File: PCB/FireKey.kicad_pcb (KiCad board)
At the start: 2 copper layers, 100 x 96.5 mm, 76 parts, among them SW1 SW_MEC_5E, U1 Arduino_Pro_Micro_USB-C

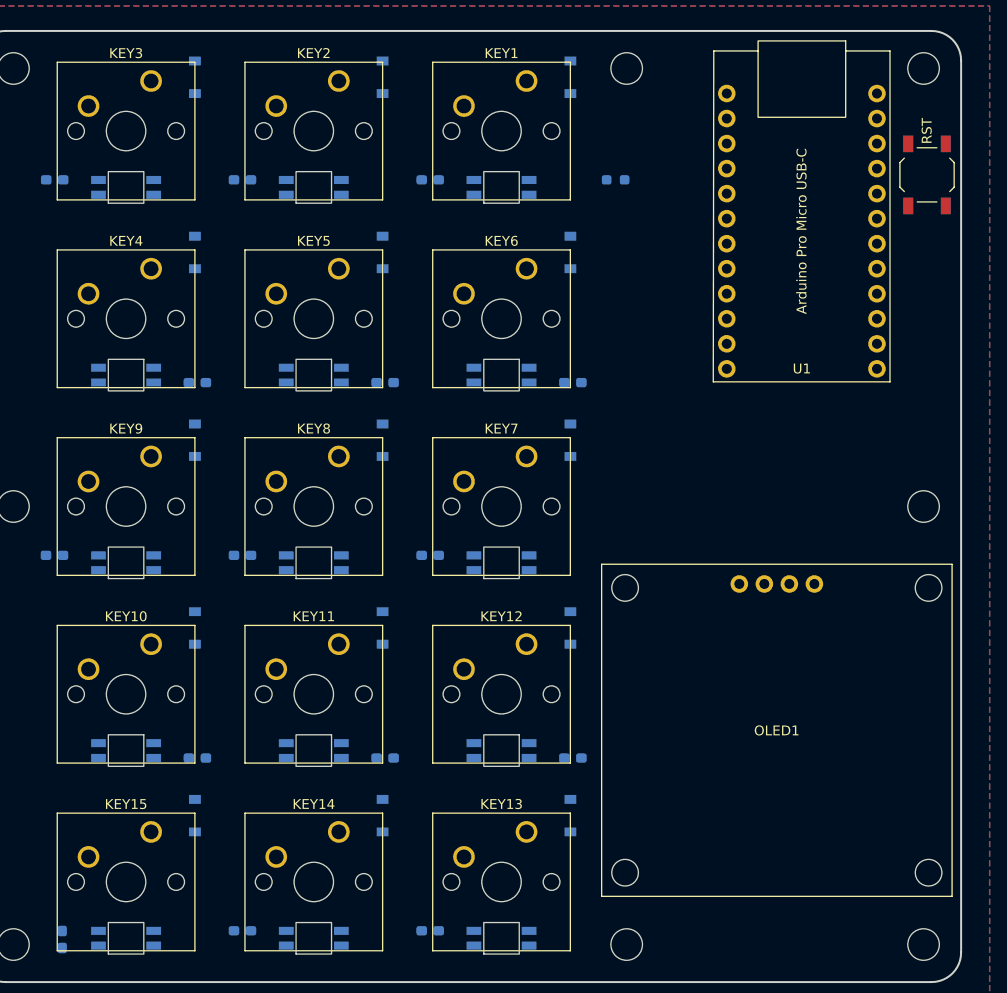
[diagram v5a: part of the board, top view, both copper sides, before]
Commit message: started routing pcb
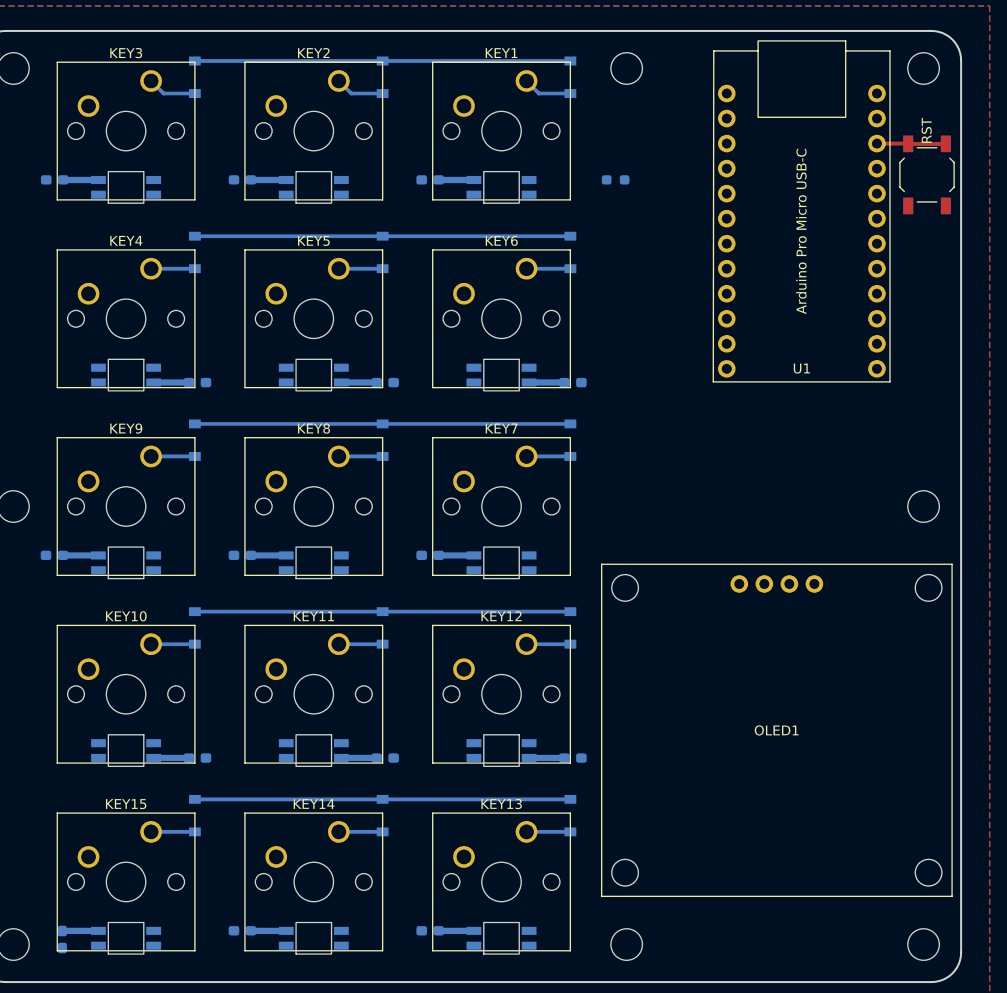
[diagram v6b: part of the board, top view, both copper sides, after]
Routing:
- net VCC: track 0.00 -> 54.2 mm
- net Row4: track 0.00 -> 38.1 mm
- net Row3: track 0.00 -> 38.1 mm
- net Row2: track 0.00 -> 38.1 mm
- net Row1: track 0.00 -> 38.1 mm
- net Row0: track 0.00 -> 38.1 mm
- net RST: track 0.00 -> 6.99 mm
- net Net-(D1-Pad2): track 0.00 -> 4.97 mm
- net Net-(D3-Pad2): track 0.00 -> 4.97 mm
- net Net-(D2-Pad2): track 0.00 -> 4.97 mm
- net Net-(D7-Pad2): track 0.00 -> 4.45 mm
- net Net-(D6-Pad2): track 0.00 -> 4.45 mm
- net Net-(D13-Pad2): track 0.00 -> 4.45 mm
- net Net-(D12-Pad2): track 0.00 -> 4.45 mm
- net Net-(D9-Pad2): track 0.00 -> 4.44 mm
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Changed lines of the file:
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@@
     (effects (font (size 1 1) (thickness 0.2)) (justify mirror))
   )
-  (dimension (type aligned) (layer "B.Cu")
+  (dimension (type aligned) (layer "Cmts.User")
     (pts (xy 57.15 54.61) (xy 57.15 99.06))
     (height 13.97)
-    (gr_text "44.4500 mm" (at 41.38 76.835 90) (layer "B.Cu")
+    (gr_text "44.4500 mm" (at 41.38 76.835 90) (layer "Cmts.User")
       (effects (font (size 1.5 1.5) (thickness 0.3)))
     )
@@
     (style (thickness 0.2) (arrow_length 1.27) (text_position_mode 0) (extension_height 0.58642) (extension_offset 0.5) keep_text_aligned)
   )
-  (dimension (type aligned) (layer "B.Cu")
+  (dimension (type aligned) (layer "Cmts.User")
     (pts (xy 153.32 53.8) (xy 53.34 53.8))
     (height 15.699999)
-    (gr_text "99.9800 mm" (at 103.33 36.300001) (layer "B.Cu")
+    (gr_text "99.9800 mm" (at 103.33 36.300001) (layer "Cmts.User")
       (effects (font (size 1.5 1.5) (thickness 0.3)))
     )
@@
     (style (thickness 0.2) (arrow_length 1.27) (text_position_mode 0) (extension_height 0.58642) (extension_offset 0.5) keep_text_aligned)
   )
-  (dimension (type aligned) (layer "B.Cu")
+  (dimension (type aligned) (layer "Cmts.User")
     (pts (xy 56.34 50.8) (xy 56.34 147.32))
     (height 18.24)
-    (gr_text "96.5200 mm" (at 36.3 99.06 90) (layer "B.Cu")
+    (gr_text "96.5200 mm" (at 36.3 99.06 90) (layer "Cmts.User")
       (effects (font (size 1.5 1.5) (thickness 0.3)))
     )
@@
     (style (thickness 0.2) (arrow_length 1.27) (text_position_mode 0) (extension_height 0.58642) (extension_offset 0.5) keep_text_aligned)
   )
-  (dimension (type aligned) (layer "B.Cu")
+  (dimension (type aligned) (layer "Cmts.User")
     (pts (xy 119.38 54.61) (xy 57.15 54.61))
     (height 11.43)
-    (gr_text "62.2300 mm" (at 88.265 41.38) (layer "B.Cu")
+    (gr_text "62.2300 mm" (at 88.265 41.38) (layer "Cmts.User")
       (effects (font (size 1.5 1.5) (thickness 0.3)))
     )
@@
     (style (thickness 0.2) (arrow_length 1.27) (text_position_mode 0) (extension_height 0.58642) (extension_offset 0.5) keep_text_aligned)
   )
-  (dimension (type aligned) (layer "B.Cu")
+  (dimension (type aligned) (layer "Cmts.User")
     (pts (xy 57.15 143.51) (xy 57.15 99.06))
     (height -13.97)
-    (gr_text "44.4500 mm" (at 41.38 121.285 90) (layer "B.Cu")
+    (gr_text "44.4500 mm" (at 41.38 121.285 90) (layer "Cmts.User")
       (effects (font (size 1.5 1.5) (thickness 0.3)))
     )
@@
     (style (thickness 0.2) (arrow_length 1.27) (text_position_mode 0) (extension_height 0.58642) (extension_offset 0.5) keep_text_aligned)
   )
-  (dimension (type aligned) (layer "B.Cu")
+  (dimension (type aligned) (layer "Cmts.User")
     (pts (xy 149.51 54.61) (xy 119.38 54.61))
     (height 11.43)
-    (gr_text "30.1300 mm" (at 134.445 41.38) (layer "B.Cu")
+    (gr_text "30.1300 mm" (at 134.445 41.38) (layer "Cmts.User")
       (effects (font (size 1.5 1.5) (thickness 0.3)))
     )
@@
     (style (thickness 0.2) (arrow_length 1.27) (text_position_mode 0) (extension_height 0.58642) (extension_offset 0.5) keep_text_aligned)
   )
+  (segment (start 62.1175 142.125) (end 62.103 142.1395) (width 0.635) (layer "B.Cu") (net 1))
+  (segment (start 93.9945 86.475) (end 94.0065 86.487) (width 0.635) (layer "B.Cu") (net 1))
+  (segment (start 62.189 104.025) (end 62.177 104.013) (width 0.635) (layer "B.Cu") (net 1))
+  (segment (start 81.2655 65.925) (end 81.2535 65.913) (width 0.635) (layer "B.Cu") (net 1))
+  (segment (start 65.78 65.925) (end 62.2155 65.925) (width 0.635) (layer "B.Cu") (net 1))
+  (segment (start 100.3155 65.925) (end 100.3035 65.913) (width 0.635) (layer "B.Cu") (net 1))
+  (segment (start 65.78 104.025) (end 62.189 104.025) (width 0.635) (layer "B.Cu") (net 1))
+  (segment (start 109.48 86.475) (end 113.0445 86.475) (width 0.635) (layer "B.Cu") (net 1))
+  (segment (start 71.38 124.575) (end 74.9445 124.575) (width 0.635) (layer "B.Cu") (net 1))
+  (segment (start 100.3155 142.125) (end 100.3035 142.113) (width 0.635) (layer "B.Cu") (net 1))
+  (segment (start 84.83 142.125) (end 81.2655 142.125) (width 0.635) (layer "B.Cu") (net 1))
+  (segment (start 113.0445 86.475) (end 113.0565 86.487) (width 0.635) (layer "B.Cu") (net 1))
+  (segment (start 103.88 142.125) (end 100.3155 142.125) (width 0.635) (layer "B.Cu") (net 1))
+  (segment (start 81.2655 104.025) (end 81.2535 104.013) (width 0.635) (layer "B.Cu") (net 1))
+  (segment (start 90.43 86.475) (end 93.9945 86.475) (width 0.635) (layer "B.Cu") (net 1))
+  (segment (start 100.445 104.025) (end 100.33 104.14) (width 0.635) (layer "B.Cu") (net 1))
+  (segment (start 84.83 104.025) (end 81.2655 104.025) (width 0.635) (layer "B.Cu") (net 1))
+  (segment (start 103.88 65.925) (end 100.3155 65.925) (width 0.635) (layer "B.Cu") (net 1))
+  (segment (start 62.2155 65.925) (end 62.2035 65.913) (width 0.635) (layer "B.Cu") (net 1))
+  (segment (start 113.0445 124.575) (end 113.0565 124.587) (width 0.635) (layer "B.Cu") (net 1))
+  (segment (start 109.48 124.575) (end 113.0445 124.575) (width 0.635) (layer "B.Cu") (net 1))
+  (segment (start 81.2655 142.125) (end 81.2535 142.113) (width 0.635) (layer "B.Cu") (net 1))
+  (segment (start 93.9945 124.575) (end 94.0065 124.587) (width 0.635) (layer "B.Cu") (net 1))
+  (segment (start 71.38 86.475) (end 74.9445 86.475) (width 0.635) (layer "B.Cu") (net 1))
+  (segment (start 90.43 124.575) (end 93.9945 124.575) (width 0.635) (layer "B.Cu") (net 1))
+  (segment (start 100.3155 104.025) (end 100.3035 104.013) (width 0.635) (layer "B.Cu") (net 1))
+  (segment (start 84.83 65.925) (end 81.2655 65.925) (width 0.635) (layer "B.Cu") (net 1))
+  (segment (start 62.345 104.025) (end 62.23 104.14) (width 0.635) (layer "B.Cu") (net 1))
+  (segment (start 65.78 142.125) (end 62.1175 142.125) (width 0.635) (layer "B.Cu") (net 1))
+  (segment (start 74.9445 124.575) (end 74.9565 124.587) (width 0.635) (layer "B.Cu") (net 1))
+  (segment (start 74.9445 86.475) (end 74.9565 86.487) (width 0.635) (layer "B.Cu") (net 1))
+  (segment (start 103.88 104.025) (end 100.3155 104.025) (width 0.635) (layer "B.Cu") (net 1))
+  (segment (start 94.615 53.85) (end 113.665 53.85) (width 0.381) (layer "B.Cu") (net 3))
+  (segment (start 75.565 53.85) (end 94.615 53.85) (width 0.381) (layer "B.Cu") (net 3))
+  (segment (start 110.49 57.15) (end 109.22 55.88) (width 0.381) (layer "B.Cu") (net 4))
+  (segment (start 113.665 57.15) (end 110.49 57.15) (width 0.381) (layer "B.Cu") (net 4))
+  (segment (start 91.44 57.15) (end 90.17 55.88) (width 0.381) (layer "B.Cu") (net 5))
+  (segment (start 94.615 57.15) (end 91.44 57.15) (width 0.381) (layer "B.Cu") (net 5))
+  (segment (start 72.39 57.15) (end 71.12 55.88) (width 0.381) (layer "B.Cu") (net 6))
+  (segment (start 75.565 57.15) (end 72.39 57.15) (width 0.381) (layer "B.Cu") (net 6))
+  (segment (start 113.665 71.63) (end 94.615 71.63) (width 0.381) (layer "B.Cu") (net 7))
+  (segment (start 94.615 71.63) (end 75.565 71.63) (width 0.381) (layer "B.Cu") (net 7))
+  (segment (start 75.565 74.93) (end 71.12 74.93) (width 0.381) (layer "B.Cu") (net 8))
+  (segment (start 94.615 74.93) (end 90.17 74.93) (width 0.381) (layer "B.Cu") (net 9))
+  (segment (start 113.665 74.93) (end 109.22 74.93) (width 0.381) (layer "B.Cu") (net 10))
+  (segment (start 94.615 90.68) (end 113.665 90.68) (width 0.381) (layer "B.Cu") (net 11))
+  (segment (start 75.565 90.68) (end 94.615 90.68) (width 0.381) (layer "B.Cu") (net 11))
+  (segment (start 113.665 93.98) (end 109.22 93.98) (width 0.381) (layer "B.Cu") (net 12))
+  (segment (start 94.615 93.98) (end 90.17 93.98) (width 0.381) (layer "B.Cu") (net 13))
+  (segment (start 75.565 93.98) (end 71.12 93.98) (width 0.381) (layer "B.Cu") (net 14))
+  (segment (start 113.665 109.73) (end 94.615 109.73) (width 0.381) (layer "B.Cu") (net 15))
+  (segment (start 94.615 109.73) (end 75.565 109.73) (width 0.381) (layer "B.Cu") (net 15))
+  (segment (start 75.565 113.03) (end 71.12 113.03) (width 0.381) (layer "B.Cu") (net 16))
+  (segment (start 94.615 113.03) (end 90.17 113.03) (width 0.381) (layer "B.Cu") (net 17))
+  (segment (start 113.665 113.03) (end 109.22 113.03) (width 0.381) (layer "B.Cu") (net 18))
+  (segment (start 113.665 128.78) (end 94.615 128.78) (width 0.381) (layer "B.Cu") (net 19))
+  (segment (start 94.615 128.78) (end 75.565 128.78) (width 0.381) (layer "B.Cu") (net 19))
+  (segment (start 113.665 132.08) (end 109.22 132.08) (width 0.381) (layer "B.Cu") (net 20))
+  (segment (start 94.615 132.08) (end 90.17 132.08) (width 0.381) (layer "B.Cu") (net 21))
+  (segment (start 75.565 132.08) (end 71.12 132.08) (width 0.381) (layer "B.Cu") (net 22))
+  (segment (start 147.96 62.255) (end 151.76 62.255) (width 0.381) (layer "F.Cu") (net 42))
+  (segment (start 144.78 62.23) (end 147.935 62.23) (width 0.381) (layer "F.Cu") (net 42))
+  (segment (start 147.935 62.23) (end 147.96 62.255) (width 0.381) (layer "F.Cu") (net 42))
   (zone (net 2) (net_name "GND") (layers F&B.Cu) (hatch edge 0.508)
     (connect_pads (clearance 0.508))

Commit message: fixed mx switches
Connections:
- KEY1 pad 2: Net-(D1-Pad2) -> Col0
- KEY10 pad 2: Net-(D10-Pad2) -> Col2
- KEY11 pad 2: Net-(D11-Pad2) -> Col1
- KEY12 pad 2: Net-(D12-Pad2) -> Col0
- KEY13 pad 2: Net-(D13-Pad2) -> Col0
- KEY14 pad 2: Net-(D14-Pad2) -> Col1
- KEY15 pad 2: Net-(D15-Pad2) -> Col2
- KEY2 pad 2: Net-(D2-Pad2) -> Col1
- KEY3 pad 2: Net-(D3-Pad2) -> Col2
- KEY4 pad 2: Net-(D4-Pad2) -> Col2
- KEY5 pad 2: Net-(D5-Pad2) -> Col1
- KEY6 pad 2: Net-(D6-Pad2) -> Col0
- KEY7 pad 2: Net-(D7-Pad2) -> Col0
- KEY8 pad 2: Net-(D8-Pad2) -> Col1
- KEY9 pad 2: Net-(D9-Pad2) -> Col2
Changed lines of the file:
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@@
       (net 22 "Net-(D15-Pad2)") (pinfunction "A") (pintype "passive"))
     (pad "2" thru_hole circle locked (at -6.35 2.54) (size 2.2 2.2) (drill 1.5) (layers *.Cu *.Mask)
-      (net 22 "Net-(D15-Pad2)") (pinfunction "A") (pintype "passive"))
+      (net 47 "Col2") (pinfunction "B") (pintype "passive"))
     (model "${KICAD6_3DMODEL_DIR}/Button_Switch_Keyboard.3dshapes/SW_Cherry_MX_1.00u_PCB.wrl"
       (offset (xyz 0 0 0))
@@
       (net 9 "Net-(D5-Pad2)") (pinfunction "A") (pintype "passive"))
     (pad "2" thru_hole circle locked (at -6.35 2.54) (size 2.2 2.2) (drill 1.5) (layers *.Cu *.Mask)
-      (net 9 "Net-(D5-Pad2)") (pinfunction "A") (pintype "passive"))
+      (net 49 "Col1") (pinfunction "B") (pintype "passive"))
     (model "${KICAD6_3DMODEL_DIR}/Button_Switch_Keyboard.3dshapes/SW_Cherry_MX_1.00u_PCB.wrl"
       (offset (xyz 0 0 0))
@@
       (net 4 "Net-(D1-Pad2)") (pinfunction "A") (pintype "passive"))
     (pad "2" thru_hole circle locked (at -6.35 2.54) (size 2.2 2.2) (drill 1.5) (layers *.Cu *.Mask)
-      (net 4 "Net-(D1-Pad2)") (pinfunction "A") (pintype "passive"))
+      (net 46 "Col0") (pinfunction "B") (pintype "passive"))
     (model "${KICAD6_3DMODEL_DIR}/Button_Switch_Keyboard.3dshapes/SW_Cherry_MX_1.00u_PCB.wrl"
       (offset (xyz 0 0 0))
@@
       (net 8 "Net-(D4-Pad2)") (pinfunction "A") (pintype "passive"))
     (pad "2" thru_hole circle locked (at -6.35 2.54) (size 2.2 2.2) (drill 1.5) (layers *.Cu *.Mask)
-      (net 8 "Net-(D4-Pad2)") (pinfunction "A") (pintype "passive"))
+      (net 47 "Col2") (pinfunction "B") (pintype "passive"))
     (model "${KICAD6_3DMODEL_DIR}/Button_Switch_Keyboard.3dshapes/SW_Cherry_MX_1.00u_PCB.wrl"
       (offset (xyz 0 0 0))
@@
       (net 12 "Net-(D7-Pad2)") (pinfunction "A") (pintype "passive"))
     (pad "2" thru_hole circle locked (at -6.35 2.54) (size 2.2 2.2) (drill 1.5) (layers *.Cu *.Mask)
-      (net 12 "Net-(D7-Pad2)") (pinfunction "A") (pintype "passive"))
+      (net 46 "Col0") (pinfunction "B") (pintype "passive"))
     (model "${KICAD6_3DMODEL_DIR}/Button_Switch_Keyboard.3dshapes/SW_Cherry_MX_1.00u_PCB.wrl"
       (offset (xyz 0 0 0))
@@
       (net 14 "Net-(D9-Pad2)") (pinfunction "A") (pintype "passive"))
     (pad "2" thru_hole circle locked (at -6.35 2.54) (size 2.2 2.2) (drill 1.5) (layers *.Cu *.Mask)
-      (net 14 "Net-(D9-Pad2)") (pinfunction "A") (pintype "passive"))
+      (net 47 "Col2") (pinfunction "B") (pintype "passive"))
     (model "${KICAD6_3DMODEL_DIR}/Button_Switch_Keyboard.3dshapes/SW_Cherry_MX_1.00u_PCB.wrl"
       (offset (xyz 0 0 0))
@@
       (net 20 "Net-(D13-Pad2)") (pinfunction "A") (pintype "passive"))
     (pad "2" thru_hole circle locked (at -6.35 2.54) (size 2.2 2.2) (drill 1.5) (layers *.Cu *.Mask)
-      (net 20 "Net-(D13-Pad2)") (pinfunction "A") (pintype "passive"))
+      (net 46 "Col0") (pinfunction "B") (pintype "passive"))
     (model "${KICAD6_3DMODEL_DIR}/Button_Switch_Keyboard.3dshapes/SW_Cherry_MX_1.00u_PCB.wrl"
       (offset (xyz 0 0 0))
@@
       (net 16 "Net-(D10-Pad2)") (pinfunction "A") (pintype "passive"))
     (pad "2" thru_hole circle locked (at -6.35 2.54) (size 2.2 2.2) (drill 1.5) (layers *.Cu *.Mask)
-      (net 16 "Net-(D10-Pad2)") (pinfunction "A") (pintype "passive"))
+      (net 47 "Col2") (pinfunction "B") (pintype "passive"))
     (model "${KICAD6_3DMODEL_DIR}/Button_Switch_Keyboard.3dshapes/SW_Cherry_MX_1.00u_PCB.wrl"
       (offset (xyz 0 0 0))
@@
       (net 17 "Net-(D11-Pad2)") (pinfunction "A") (pintype "passive"))
     (pad "2" thru_hole circle locked (at -6.35 2.54) (size 2.2 2.2) (drill 1.5) (layers *.Cu *.Mask)
-      (net 17 "Net-(D11-Pad2)") (pinfunction "A") (pintype "passive"))
+      (net 49 "Col1") (pinfunction "B") (pintype "passive"))
     (model "${KICAD6_3DMODEL_DIR}/Button_Switch_Keyboard.3dshapes/SW_Cherry_MX_1.00u_PCB.wrl"
       (offset (xyz 0 0 0))
@@
       (net 5 "Net-(D2-Pad2)") (pinfunction "A") (pintype "passive"))
     (pad "2" thru_hole circle locked (at -6.35 2.54) (size 2.2 2.2) (drill 1.5) (layers *.Cu *.Mask)
-      (net 5 "Net-(D2-Pad2)") (pinfunction "A") (pintype "passive"))
+      (net 49 "Col1") (pinfunction "B") (pintype "passive"))
     (model "${KICAD6_3DMODEL_DIR}/Button_Switch_Keyboard.3dshapes/SW_Cherry_MX_1.00u_PCB.wrl"
       (offset (xyz 0 0 0))
@@
       (net 18 "Net-(D12-Pad2)") (pinfunction "A") (pintype "passive"))
     (pad "2" thru_hole circle locked (at -6.35 2.54) (size 2.2 2.2) (drill 1.5) (layers *.Cu *.Mask)
-      (net 18 "Net-(D12-Pad2)") (pinfunction "A") (pintype "passive"))
+      (net 46 "Col0") (pinfunction "B") (pintype "passive"))
     (model "${KICAD6_3DMODEL_DIR}/Button_Switch_Keyboard.3dshapes/SW_Cherry_MX_1.00u_PCB.wrl"
       (offset (xyz 0 0 0))
@@
       (net 6 "Net-(D3-Pad2)") (pinfunction "A") (pintype "passive"))
     (pad "2" thru_hole circle locked (at -6.35 2.54) (size 2.2 2.2) (drill 1.5) (layers *.Cu *.Mask)
-      (net 6 "Net-(D3-Pad2)") (pinfunction "A") (pintype "passive"))
+      (net 47 "Col2") (pinfunction "B") (pintype "passive"))
     (model "${KICAD6_3DMODEL_DIR}/Button_Switch_Keyboard.3dshapes/SW_Cherry_MX_1.00u_PCB.wrl"
       (offset (xyz 0 0 0))
@@
       (net 21 "Net-(D14-Pad2)") (pinfunction "A") (pintype "passive"))
     (pad "2" thru_hole circle locked (at -6.35 2.54) (size 2.2 2.2) (drill 1.5) (layers *.Cu *.Mask)
-      (net 21 "Net-(D14-Pad2)") (pinfunction "A") (pintype "passive"))
+      (net 49 "Col1") (pinfunction "B") (pintype "passive"))
     (model "${KICAD6_3DMODEL_DIR}/Button_Switch_Keyboard.3dshapes/SW_Cherry_MX_1.00u_PCB.wrl"
       (offset (xyz 0 0 0))
@@
       (net 13 "Net-(D8-Pad2)") (pinfunction "A") (pintype "passive"))
     (pad "2" thru_hole circle locked (at -6.35 2.54) (size 2.2 2.2) (drill 1.5) (layers *.Cu *.Mask)
-      (net 13 "Net-(D8-Pad2)") (pinfunction "A") (pintype "passive"))
+      (net 49 "Col1") (pinfunction "B") (pintype "passive"))
     (model "${KICAD6_3DMODEL_DIR}/Button_Switch_Keyboard.3dshapes/SW_Cherry_MX_1.00u_PCB.wrl"
       (offset (xyz 0 0 0))
@@
       (net 10 "Net-(D6-Pad2)") (pinfunction "A") (pintype "passive"))
     (pad "2" thru_hole circle locked (at -6.35 2.54) (size 2.2 2.2) (drill 1.5) (layers *.Cu *.Mask)
-      (net 10 "Net-(D6-Pad2)") (pinfunction "A") (pintype "passive"))
-    (model "${KICAD6_3DMODEL_DIR}/Button_Switch_Keyboard.3dshapes/SW_Cherry_MX_1.00u_PCB.wrl"
-      (offset (xyz 0 0 0))
+      (net 46 "Col0") (pinfunction "B") (pintype "passive"))
+    (model "${KICAD6_3DMODEL_DIR}/Button_Switch_Keyboard.3dshapes/SW_Cherry_MX_1.00u_PCB.wrl"
+      (offset (xyz 0 0 0))

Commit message: fixed rst switch
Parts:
- SW1: value SW_MEC_5E -> SW_MEC_4A
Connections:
- SW1 pad 2: RST -> GND
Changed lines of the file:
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@@
       (effects (font (size 1 1) (thickness 0.15)))
     )
-    (fp_text value "SW_MEC_5E" (at 0 3.75 90) (layer "F.Fab")
+    (fp_text value "SW_MEC_4A" (at 0 3.75 90) (layer "F.Fab")
       (effects (font (size 1 1) (thickness 0.15)))
     )
@@
       (net 42 "RST") (pinfunction "1") (pintype "passive"))
     (pad "2" smd rect (at 3.15 1.9 90) (size 1.7 1) (layers "F.Cu" "F.Paste" "F.Mask")
-      (net 42 "RST") (pinfunction "2") (pintype "passive"))
+      (net 2 "GND") (pinfunction "2") (pintype "passive"))
     (pad "2" smd rect (at -3.15 1.9 90) (size 1.7 1) (layers "F.Cu" "F.Paste" "F.Mask")
-      (net 42 "RST") (pinfunction "2") (pintype "passive"))
+      (net 2 "GND") (pinfunction "2") (pintype "passive"))
     (model "${KICAD6_3DMODEL_DIR}/Button_Switch_SMD.3dshapes/SW_SPST_TL3342.wrl"
       (offset (xyz 0 0 0))
